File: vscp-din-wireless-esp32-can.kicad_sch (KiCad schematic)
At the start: 27 parts, among them J1 Conn_Left_I2C, J2 Conn_Right_Power, J3 Conn_01x06, J4 Conn_01x02, U1 ESP32-WROOM-32D, U2 MCP2517FD-xSL, U3 SN65HVD232, Y1 4MHz

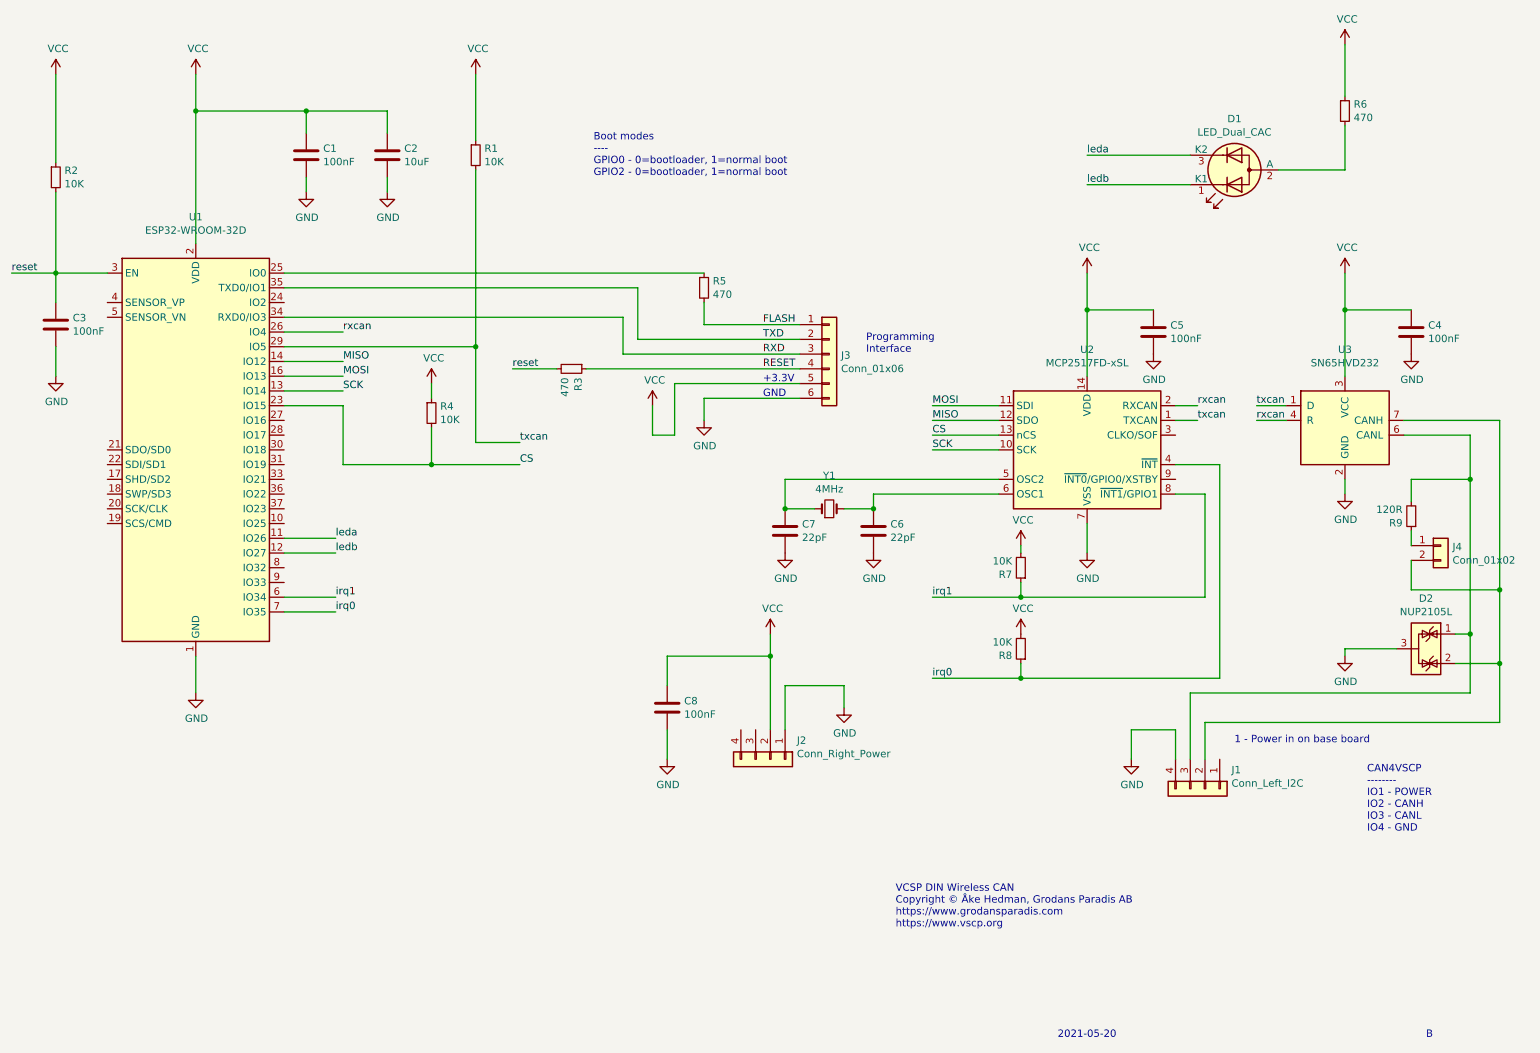
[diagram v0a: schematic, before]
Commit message: Updated ESP32 module
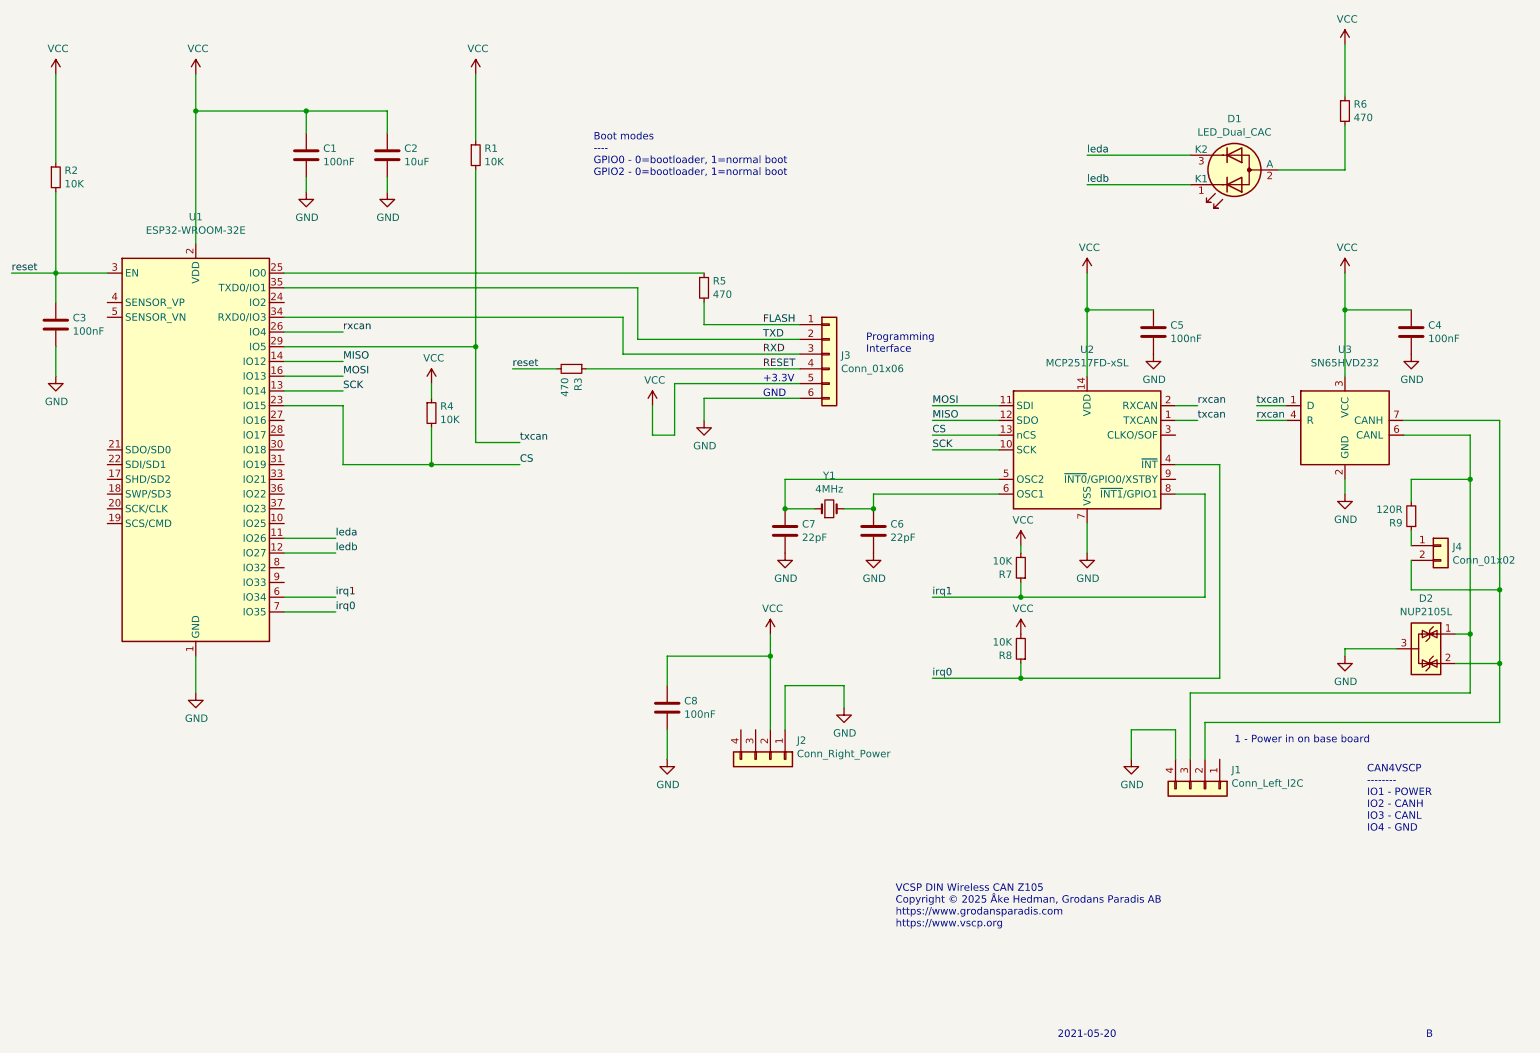
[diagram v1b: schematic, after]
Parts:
- U1: value ESP32-WROOM-32D -> ESP32-WROOM-32E
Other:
- note added: "VCSP DIN Wireless CAN Z105 Copyright © 2025 Åke Hedman, Grodans Paradis AB https://www.grodansparadis.com https://www.vscp.org"
- note removed: "VCSP DIN Wireless CAN Copyright © Åke Hedman, Grodans Paradis AB https://www.grodansparadis.com https://www.vscp.org"

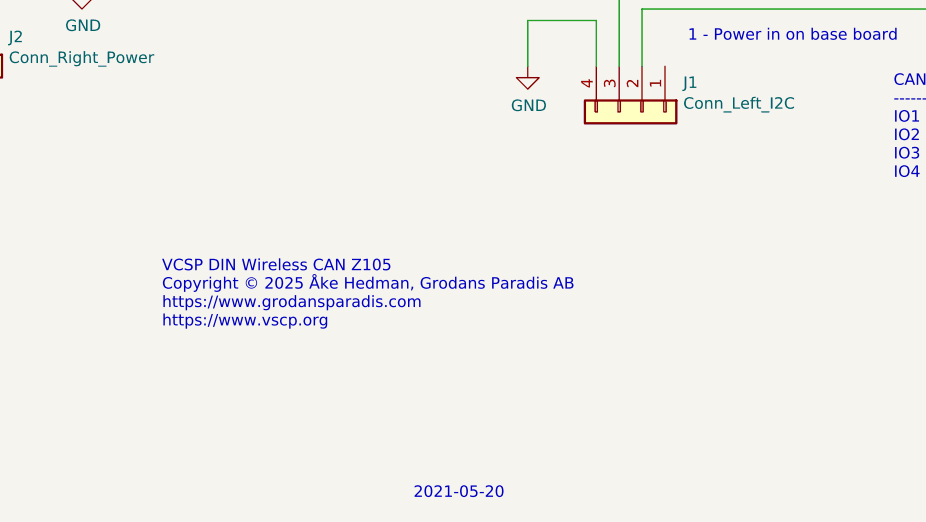
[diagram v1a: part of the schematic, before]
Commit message: Updated to KiCad version 10
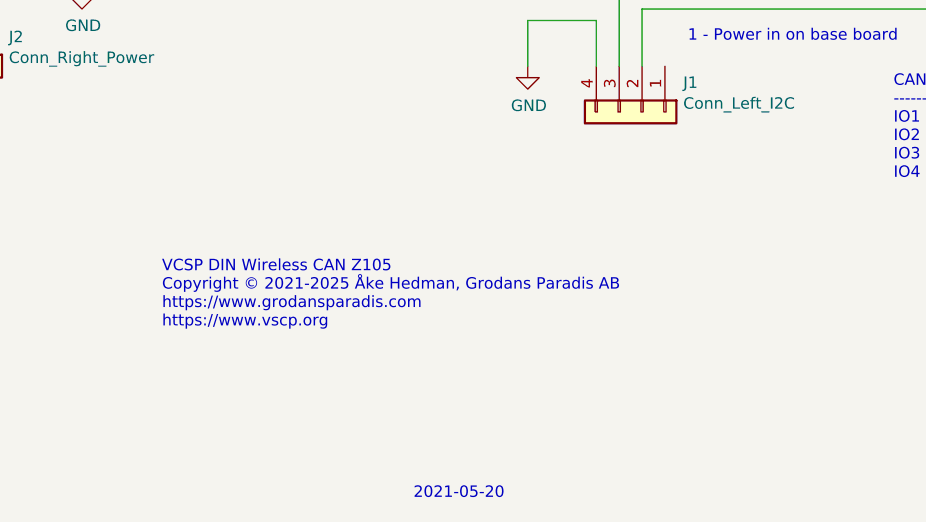
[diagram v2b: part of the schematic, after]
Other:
- note added: "VCSP DIN Wireless CAN Z105 Copyright © 2021-2025 Åke Hedman, Grodans Paradis AB https://www.grodansparadis.com https://www.vscp.org"
- note removed: "VCSP DIN Wireless CAN Z105 Copyright © 2025 Åke Hedman, Grodans Paradis AB https://www.grodansparadis.com https://www.vscp.org"
